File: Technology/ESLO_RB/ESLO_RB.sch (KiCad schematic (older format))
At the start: 65 parts, among them CN1 4700pF, CN2 1000pF, CN3 1000pF, CN4 1uF, CN5 1uF, J1 10POS Biopotentials, J2 6POS Power/JTAG, U1 MAX1720, U10 2450BM14G0011, U2 TPS62740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

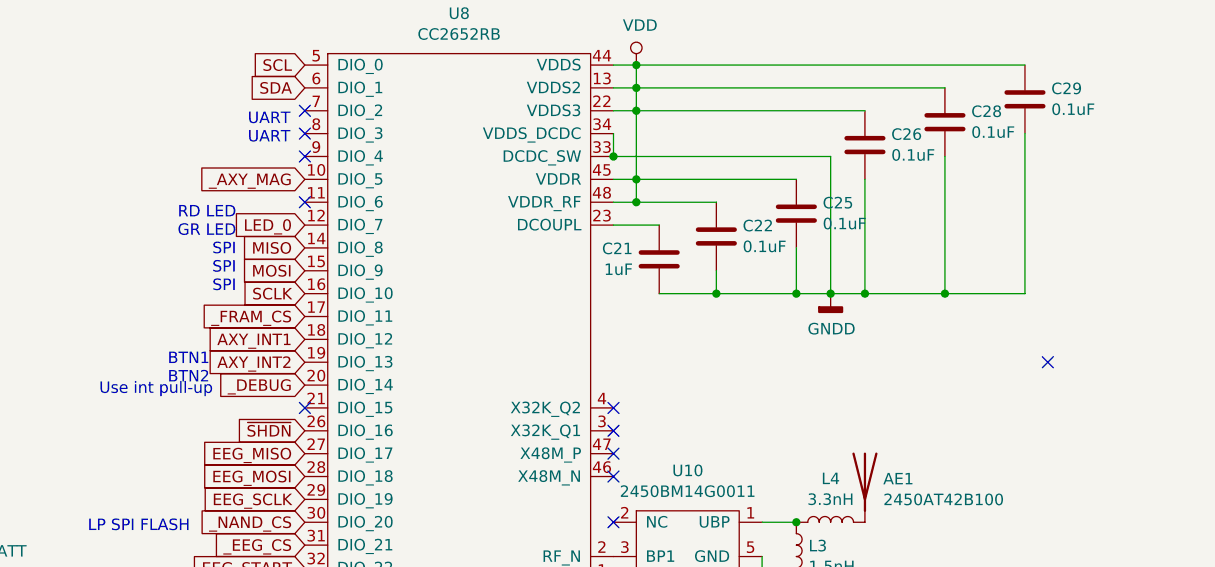
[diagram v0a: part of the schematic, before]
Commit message: Debugging ESLO PBCs
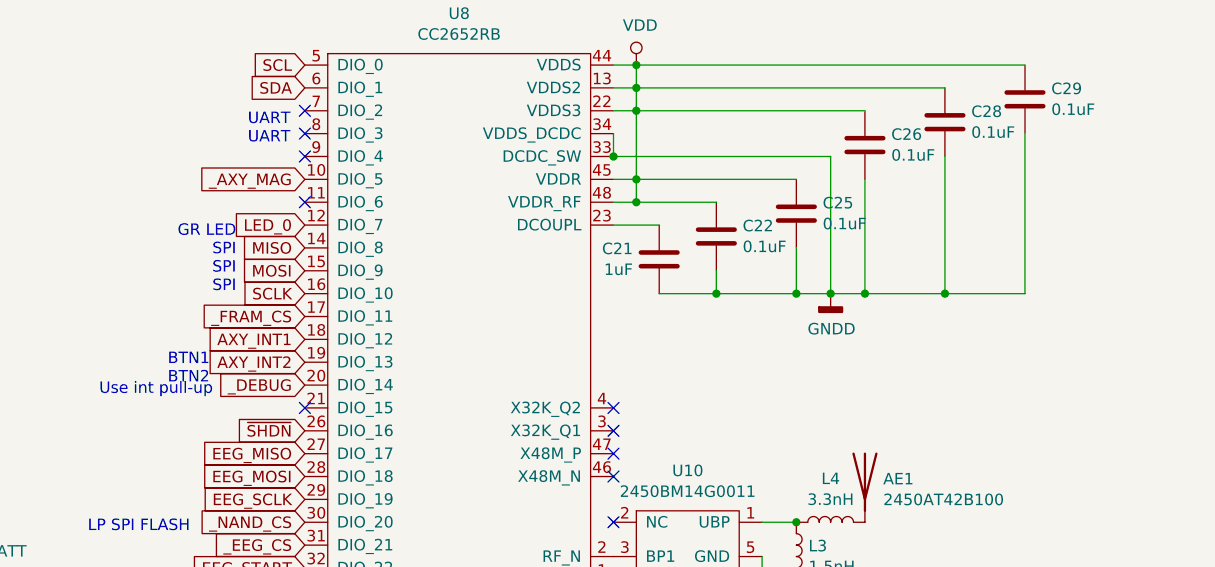
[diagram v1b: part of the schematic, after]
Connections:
- no-connect marks 18 -> 17
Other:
- note added: "GR LED\nSPI\nSPI\nSPI"
- note removed: "RD LED\nGR LED\nSPI\nSPI\nSPI"
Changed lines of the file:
@@
 Text Notes 12250 1500 0    50   ~ 0
 UART\nUART
-Text Notes 12200 2150 2    50   ~ 0
-RD LED\nGR LED\nSPI\nSPI\nSPI
 Text Notes 11900 2550 0    50   ~ 0
 BTN1\nBTN2
@@
 NoConn ~ 12500 3950
 NoConn ~ 12500 4050
-NoConn ~ 15750 2450
 Text GLabel 12500 2750 0    50   Input ~ 0
 ~SHDN
@@
 Text Notes 3450 4200 0    50   ~ 0
 10nF = 10000pF
+Text Notes 12200 2150 2    50   ~ 0
+GR LED\nSPI\nSPI\nSPI
 $EndSCHEMATC

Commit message: Debugging
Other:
- note added: "*Need these for initial program/debug"
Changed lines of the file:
@@
 Text Notes 5150 1150 0    50   ~ 0
 SHARED CAP
-Text Notes 12250 1500 0    50   ~ 0
-UART\nUART
 Text Notes 11900 2550 0    50   ~ 0
 BTN1\nBTN2
@@
 Text Notes 12200 2150 2    50   ~ 0
 GR LED\nSPI\nSPI\nSPI
+Text Notes 14150 4800 0    50   ~ 0
+*Need these for initial program/debug
+Text Notes 12250 1500 0    50   ~ 0
+UART\nUART
 $EndSCHEMATC

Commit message: Notes
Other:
- note added: "X These are actually 0.1uF, 1uF doesn’t exist"
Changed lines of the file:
@@
 Text Notes 12250 1500 0    50   ~ 0
 UART\nUART
+Text Notes 9950 8150 0    50   ~ 0
+X These are actually 0.1uF, 1uF doesn’t exist
 $EndSCHEMATC

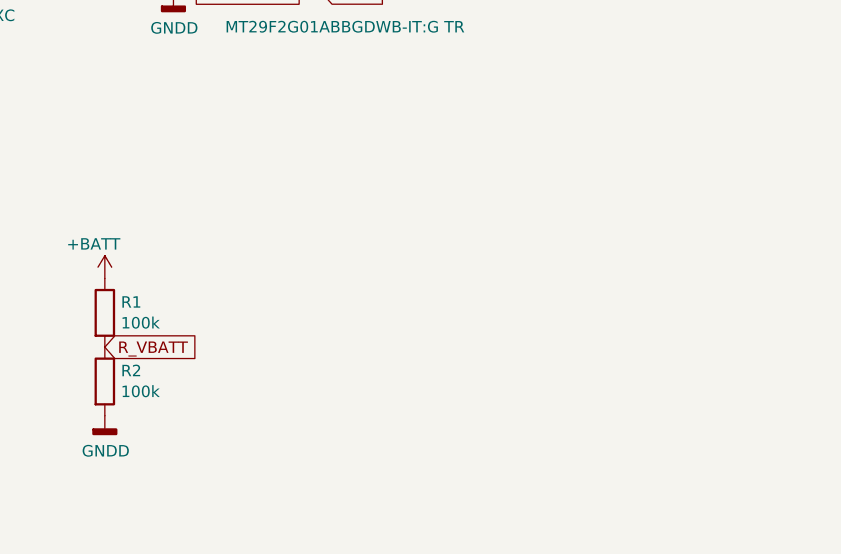
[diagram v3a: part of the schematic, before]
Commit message: Updated note on ESLO_RB
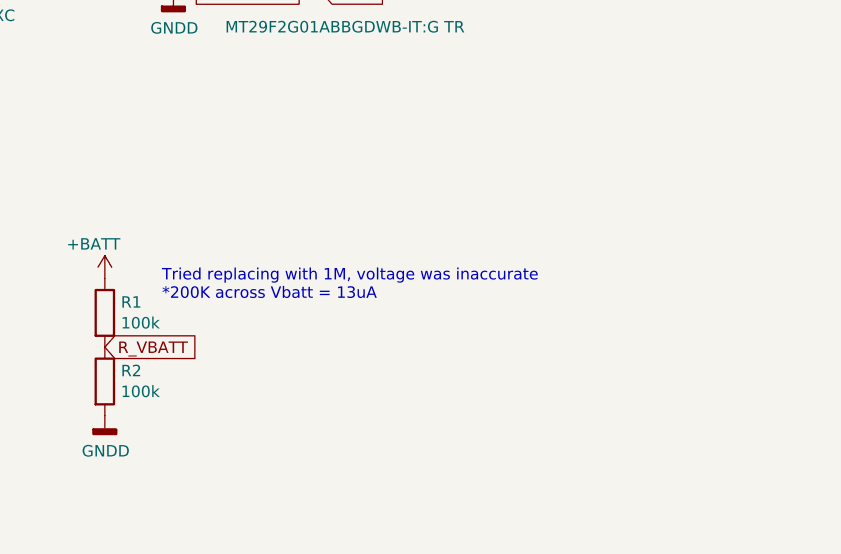
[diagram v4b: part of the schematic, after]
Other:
- note added: "Tried replacing with 1M, voltage was inaccurate\n*200K across Vbatt = 13uA"
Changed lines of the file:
@@
 Text Notes 9950 8150 0    50   ~ 0
 X These are actually 0.1uF, 1uF doesn’t exist
+Text Notes 3350 8650 0    50   ~ 0
+Tried replacing with 1M, voltage was inaccurate\n*200K across Vbatt = 13uA
 $EndSCHEMATC
